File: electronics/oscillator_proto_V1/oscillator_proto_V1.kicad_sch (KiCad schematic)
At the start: 34 parts, among them J1 module_2x15_left_input, J2 module_2x15_right_input, J3 Coax, U1 TL081, U2 LME49720, U3 TL082

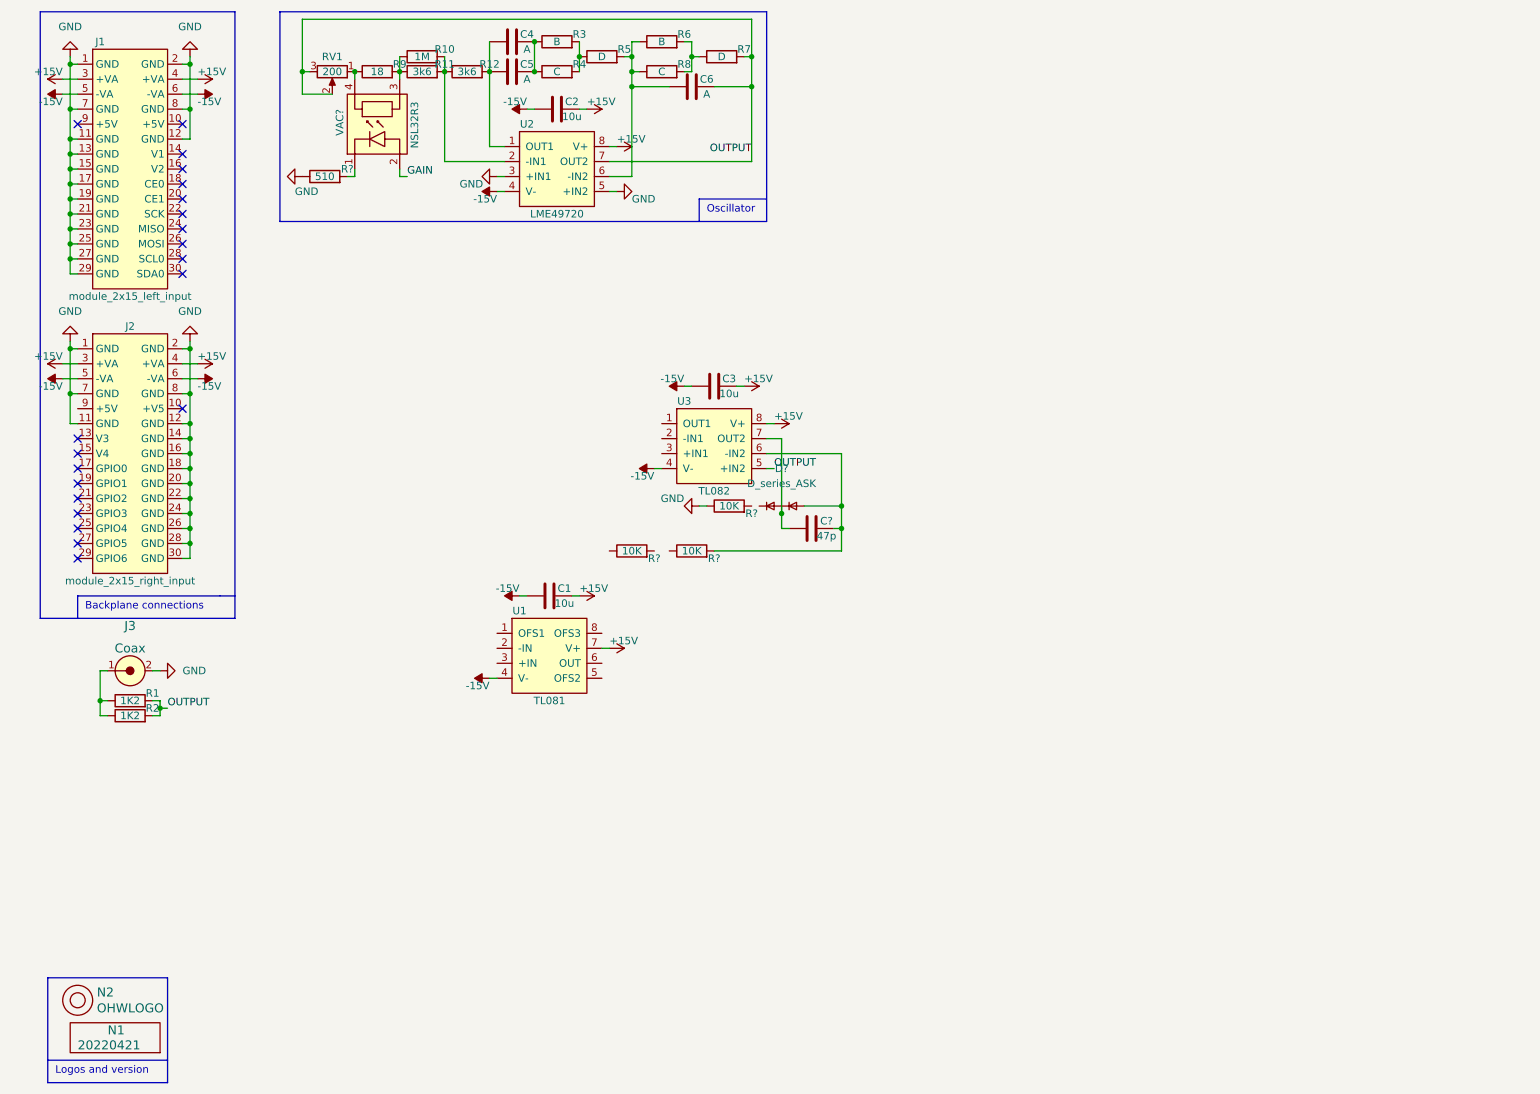
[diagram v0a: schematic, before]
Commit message: layout completed on prototype oscillator prototype
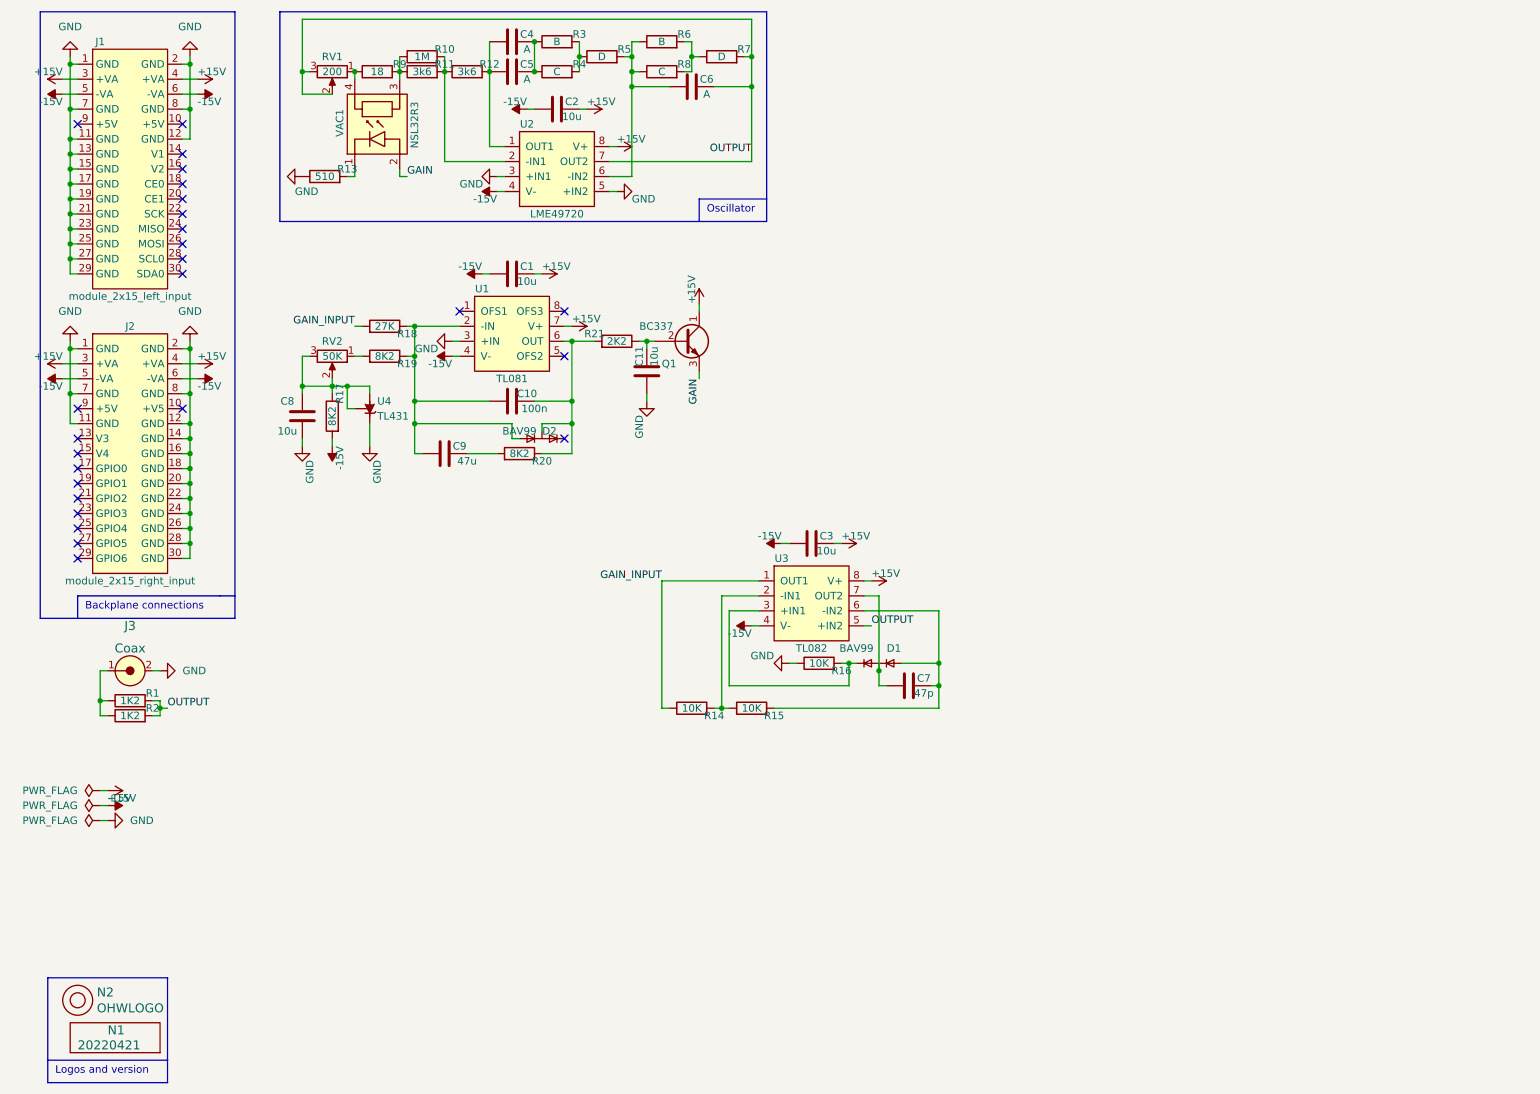
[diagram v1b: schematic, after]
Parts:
- added C10: 100n, SquantorRcl:C-025_050-030X100-film, symbol Device:C
- added C11, C8: 10u, SquantorRcl:C_0805+0603, symbol Device:C
- added C9: 47u, SquantorRcl:C-025_050-030X100-film, symbol Device:C
- added D2: BAV99, SquantorIC:SOT23-3, symbol SquantorDevice:D_series_ASK
- added Q1: BC337, Package_TO_SOT_THT:TO-92L_Inline_Wide, symbol Device:Q_NPN_CBE
- added R17, R19, R20: 8K2, SquantorRcl:R_0805+0603, symbol Device:R
- added R18: 27K, SquantorRcl:R_0805+0603, symbol Device:R
- added R21: 2K2, SquantorRcl:R_0805+0603, symbol Device:R
- added RV2: 50K, Potentiometer_THT:Potentiometer_Bourns_3296W_Vertical, symbol Device:R_Potentiometer
- added U4: TL431, Package_TO_SOT_THT:TO-92_Inline_Wide, symbol Reference_Voltage:TL431LP
- D1: renamed from D?; value D_series_ASK -> BAV99; footprint (none) -> SquantorIC:SOT23-3
- VAC1: renamed from VAC?; footprint (none) -> SquantorOpto:NSL32SR3
- gave numbers to parts that had none: 5
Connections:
- net +15V: now also Q1.1 (C)
- net -15V: now also R17.2
- net GAIN: now also Q1.3 (E)
- net GND: now also U1.3 (+IN), C11.1, C8.1, U4.3 (K)
- net GAIN_INPUT: now reaches R14.1
- net GAIN_INPUT: now also U3.1 (OUT1), R18.2
- net at R14.2: now also R15.1, U3.2 (-IN1)
- net at U3.3 (+IN1): now also D1.2 (K2), R16.2
- net at C7.1, U3.7 (OUT2): now also D1.3 (K1A2); no longer D1.2 (K1A2)
- net at U1.2 (-IN): now also C10.1, C9.1, D2.1 (A1), R18.1, R19.1
- net at U1.6 (OUT): now also C10.2, D2.3 (K1A2), R20.1, R21.2
- new net: C9.2, R20.2
- new net: R19.2, RV2.1
- new net: C8.2, R17.1, RV2.2, RV2.3, U4.1 (REF), U4.2 (A)
- new net: C11.2, Q1.2 (B), R21.1
- no-connect marks 21 -> 26
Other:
- moved on the sheet: C1, C3, C7, D1, R14, R15, R16, U1, U3

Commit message: updated resistor values and some minor routing updates
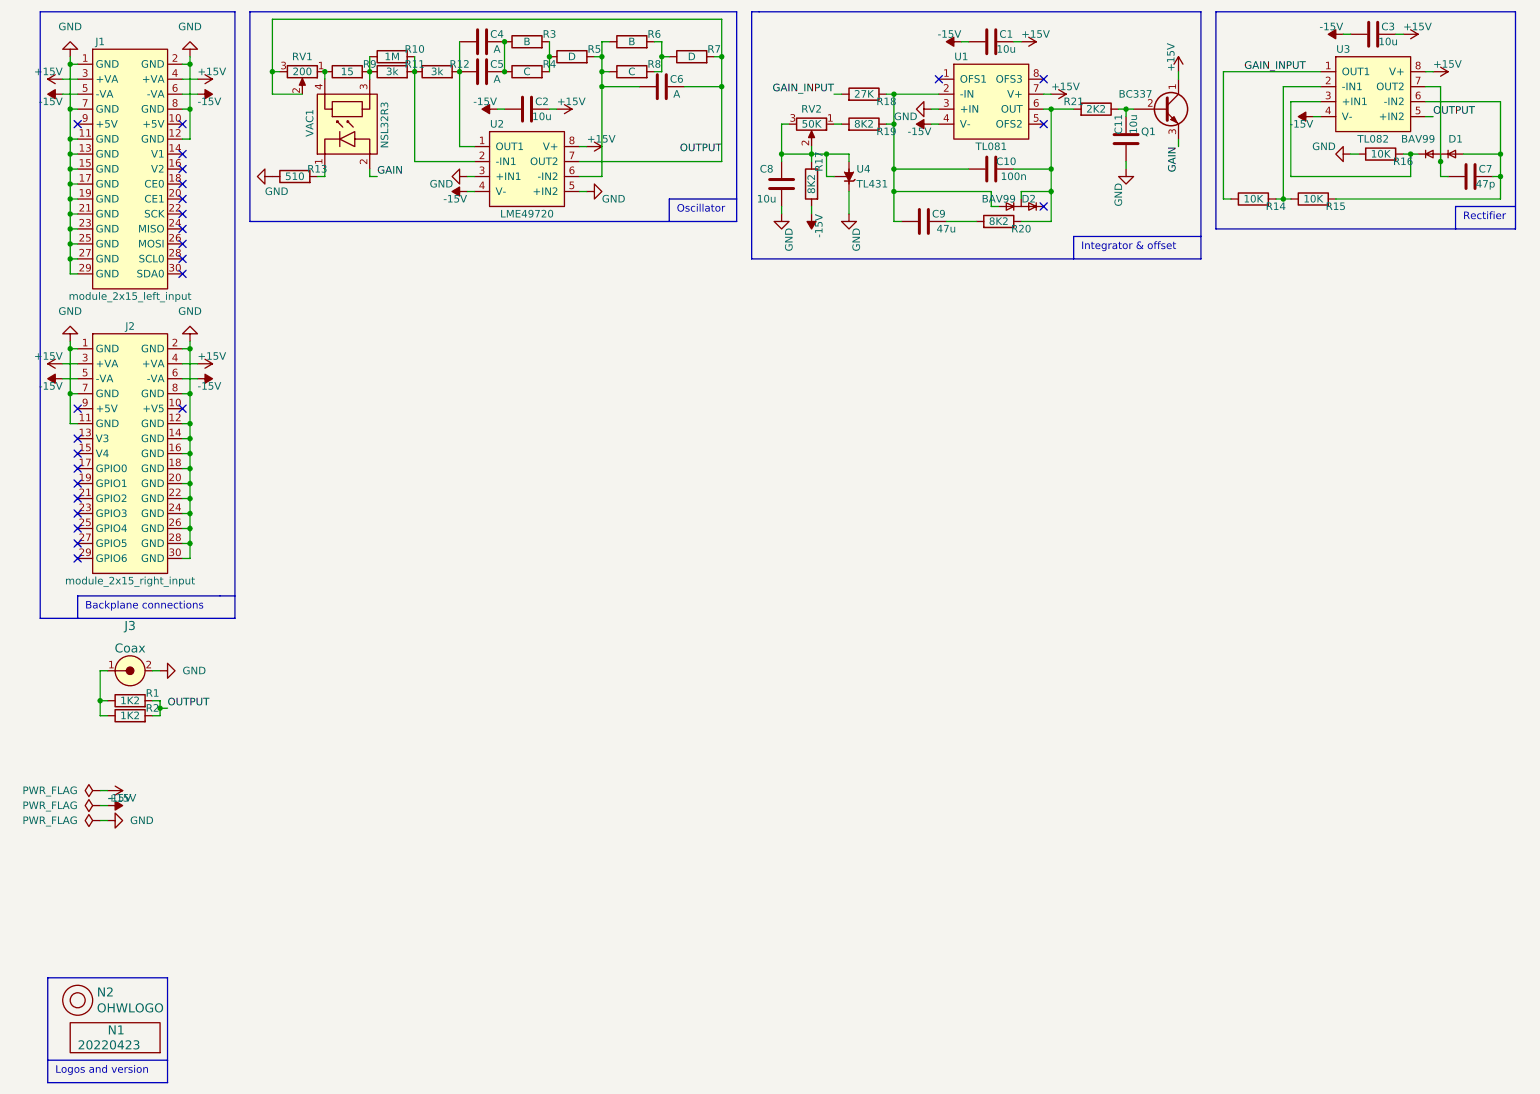
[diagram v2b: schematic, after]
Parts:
- N1: value 20220421 -> 20220423
- R11, R12: value 3k6 -> 3k
- R9: value 18 -> 15
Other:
- note added: "Integrator & offset"
- note added: "Rectifier"
- moved on the sheet: C1, C10, C11, C2, C3, C4, C5, C6, C7, C8, C9, D1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

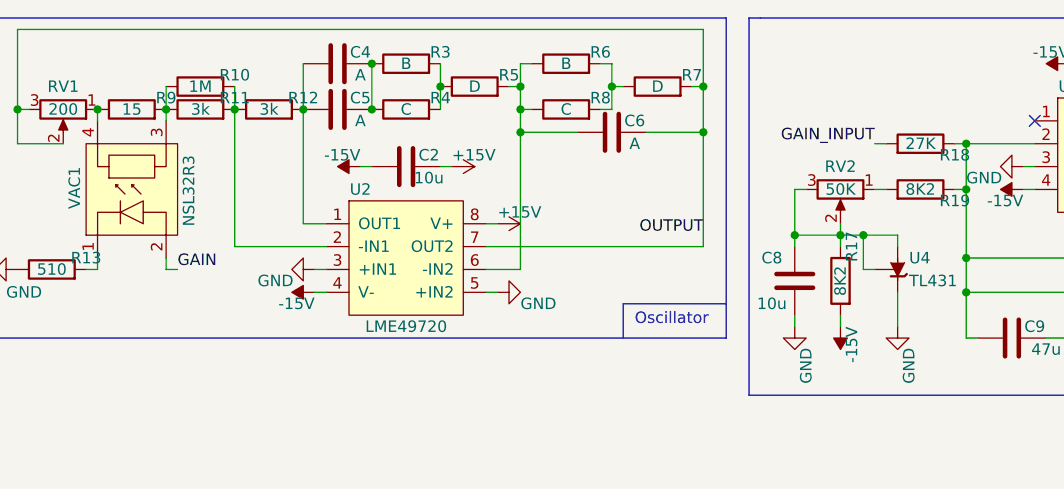
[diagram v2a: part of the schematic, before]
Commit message: fixed errors with proto oscillator
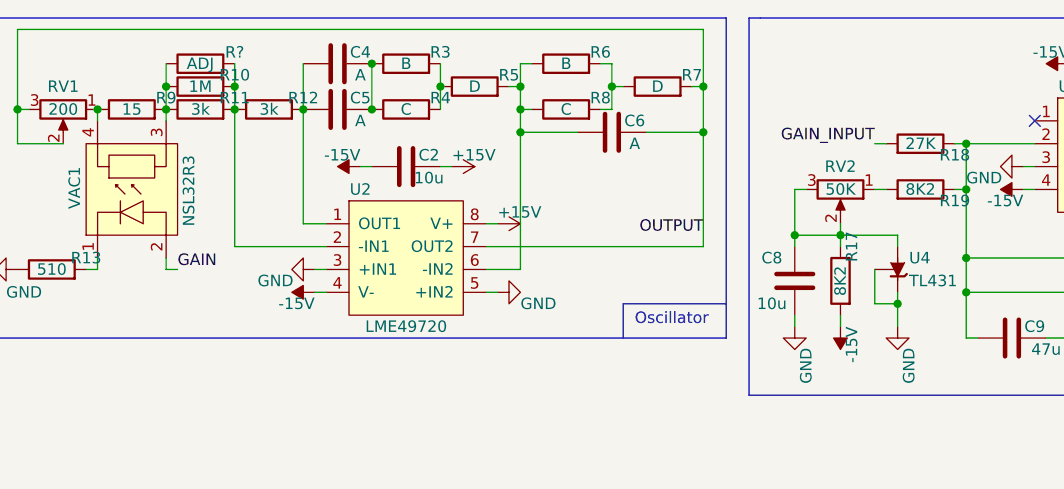
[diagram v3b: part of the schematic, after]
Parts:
- added R?: ADJ, SquantorRcl:R_0805+0603, symbol Device:R
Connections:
- net GND: now also U4.1 (REF)
- net at R10.1, R11.1, R9.2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: now also R?.1
- net at R10.2, R11.2, R12.1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: now also R?.2
- net at C8.2, R17.1, RV2.2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: no longer U4.1 (REF)
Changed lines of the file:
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@@
   (junction (at 53.34 24.13) (diameter 0) (color 0 0 0 0)
   )
+  (junction (at 77.47 21.59) (diameter 0) (color 0 0 0 0)
+  )
   (junction (at 39.37 101.6) (diameter 0) (color 0 0 0 0)
   )
+  (junction (at 69.85 21.59) (diameter 0) (color 0 0 0 0)
+  )
   (junction (at 92.71 24.13) (diameter 0) (color 0 0 0 0)
   )
@@
   (junction (at 19.05 53.34) (diameter 0) (color 0 0 0 0)
   )
-  (junction (at 147.32 38.1) (diameter 0) (color 0 0 0 0)
-  )
   (junction (at 69.85 24.13) (diameter 0) (color 0 0 0 0)
   )
@@
   )
   (junction (at 39.37 86.36) (diameter 0) (color 0 0 0 0)
+  )
+  (junction (at 151.13 45.72) (diameter 0) (color 0 0 0 0)
   )
   (junction (at 198.12 30.48) (diameter 0) (color 0 0 0 0)
@@
     (stroke (width 0) (type default) (color 0 0 0 0))
   )
-  (wire (pts (xy 148.59 41.91) (xy 147.32 41.91))
-    (stroke (width 0) (type default) (color 0 0 0 0))
-  )
   (wire (pts (xy 139.7 33.02) (xy 139.7 38.1))
     (stroke (width 0) (type default) (color 0 0 0 0))
@@
     (stroke (width 0) (type default) (color 0 0 0 0))
   )
+  (wire (pts (xy 151.13 45.72) (xy 148.59 45.72))
+    (stroke (width 0) (type default) (color 0 0 0 0))
+  )
   (wire (pts (xy 105.41 44.45) (xy 106.68 44.45))
     (stroke (width 0) (type default) (color 0 0 0 0))
@@
     (stroke (width 0) (type default) (color 0 0 0 0))
   )
-  (wire (pts (xy 144.78 38.1) (xy 147.32 38.1))
+  (wire (pts (xy 144.78 38.1) (xy 151.13 38.1))
     (stroke (width 0) (type default) (color 0 0 0 0))
   )
@@
     (stroke (width 0) (type default) (color 0 0 0 0))
   )
-  (wire (pts (xy 151.13 44.45) (xy 151.13 48.26))
+  (wire (pts (xy 151.13 44.45) (xy 151.13 45.72))
     (stroke (width 0) (type default) (color 0 0 0 0))
   )
@@
     (stroke (width 0) (type default) (color 0 0 0 0))
   )
+  (wire (pts (xy 151.13 45.72) (xy 151.13 48.26))
+    (stroke (width 0) (type default) (color 0 0 0 0))
+  )
   (wire (pts (xy 17.78 76.2) (xy 20.32 76.2))
     (stroke (width 0) (type default) (color 0 0 0 0))
@@
     (stroke (width 0) (type default) (color 0 0 0 0))
   )
-  (wire (pts (xy 147.32 38.1) (xy 147.32 41.91))
-    (stroke (width 0) (type default) (color 0 0 0 0))
-  )
   (wire (pts (xy 119.38 21.59) (xy 120.65 21.59))
     (stroke (width 0) (type default) (color 0 0 0 0))
@@
     (stroke (width 0) (type default) (color 0 0 0 0))
   )
+  (wire (pts (xy 148.59 45.72) (xy 148.59 41.91))
+    (stroke (width 0) (type default) (color 0 0 0 0))
+  )
   (wire (pts (xy 19.05 35.56) (xy 20.32 35.56))
     (stroke (width 0) (type default) (color 0 0 0 0))
@@
     (stroke (width 0) (type default) (color 0 0 0 0))
   )
+  (wire (pts (xy 77.47 19.05) (xy 77.47 21.59))
+    (stroke (width 0) (type default) (color 0 0 0 0))
+  )
   (wire (pts (xy 19.05 83.82) (xy 19.05 78.74))
     (stroke (width 0) (type default) (color 0 0 0 0))
@@
     (stroke (width 0) (type default) (color 0 0 0 0))
   )
-  (wire (pts (xy 147.32 38.1) (xy 151.13 38.1))
-    (stroke (width 0) (type default) (color 0 0 0 0))
-  )
   (wire (pts (xy 139.7 38.1) (xy 144.78 38.1))
+    (stroke (width 0) (type default) (color 0 0 0 0))
+  )
+  (wire (pts (xy 69.85 19.05) (xy 69.85 21.59))
     (stroke (width 0) (type default) (color 0 0 0 0))
   )
@@
     )
     (pin "1")
+  )
+  (symbol (lib_id "Device:R") (at 73.66 19.05 90) (unit 1)
+    (in_bom yes) (on_board yes)
+    (property "Reference" "R?" (id 0) (at 77.47 17.78 90))
+    (property "Value" "ADJ" (id 1) (at 73.66 19.05 90))
+    (property "Footprint" "SquantorRcl:R_0805+0603" (id 2) (at 73.66 20.828 90)
+      (effects (font (size 1.27 1.27)) hide)
+    )
+    (property "Datasheet" "~" (id 3) (at 73.66 19.05 0)
+      (effects (font (size 1.27 1.27)) hide)
+    )
+    (pin "1")
+    (pin "2")
   )
   (symbol (lib_id "Device:R") (at 176.53 49.53 270) (mirror x) (unit 1)
@@
       (reference "R21") (unit 1) (value "2K2") (footprint "SquantorRcl:R_0805+0603")
     )
+    (path "/21f01333-f32c-4c7a-b25c-e4d5d4e4359a"
+      (reference "R?") (unit 1) (value "ADJ") (footprint "SquantorRcl:R_0805+0603")
+    )
     (path "/afdcc91f-3c54-4dc6-8d8a-38d6d5d4d261"
